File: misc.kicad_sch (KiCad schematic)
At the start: 23 parts, among them J7 Conn_ARM_JTAG_SWD_10, SW2 SW_DIP_x02, U1 MIMX8MM6DVTLZAA, Y3 24Mhz

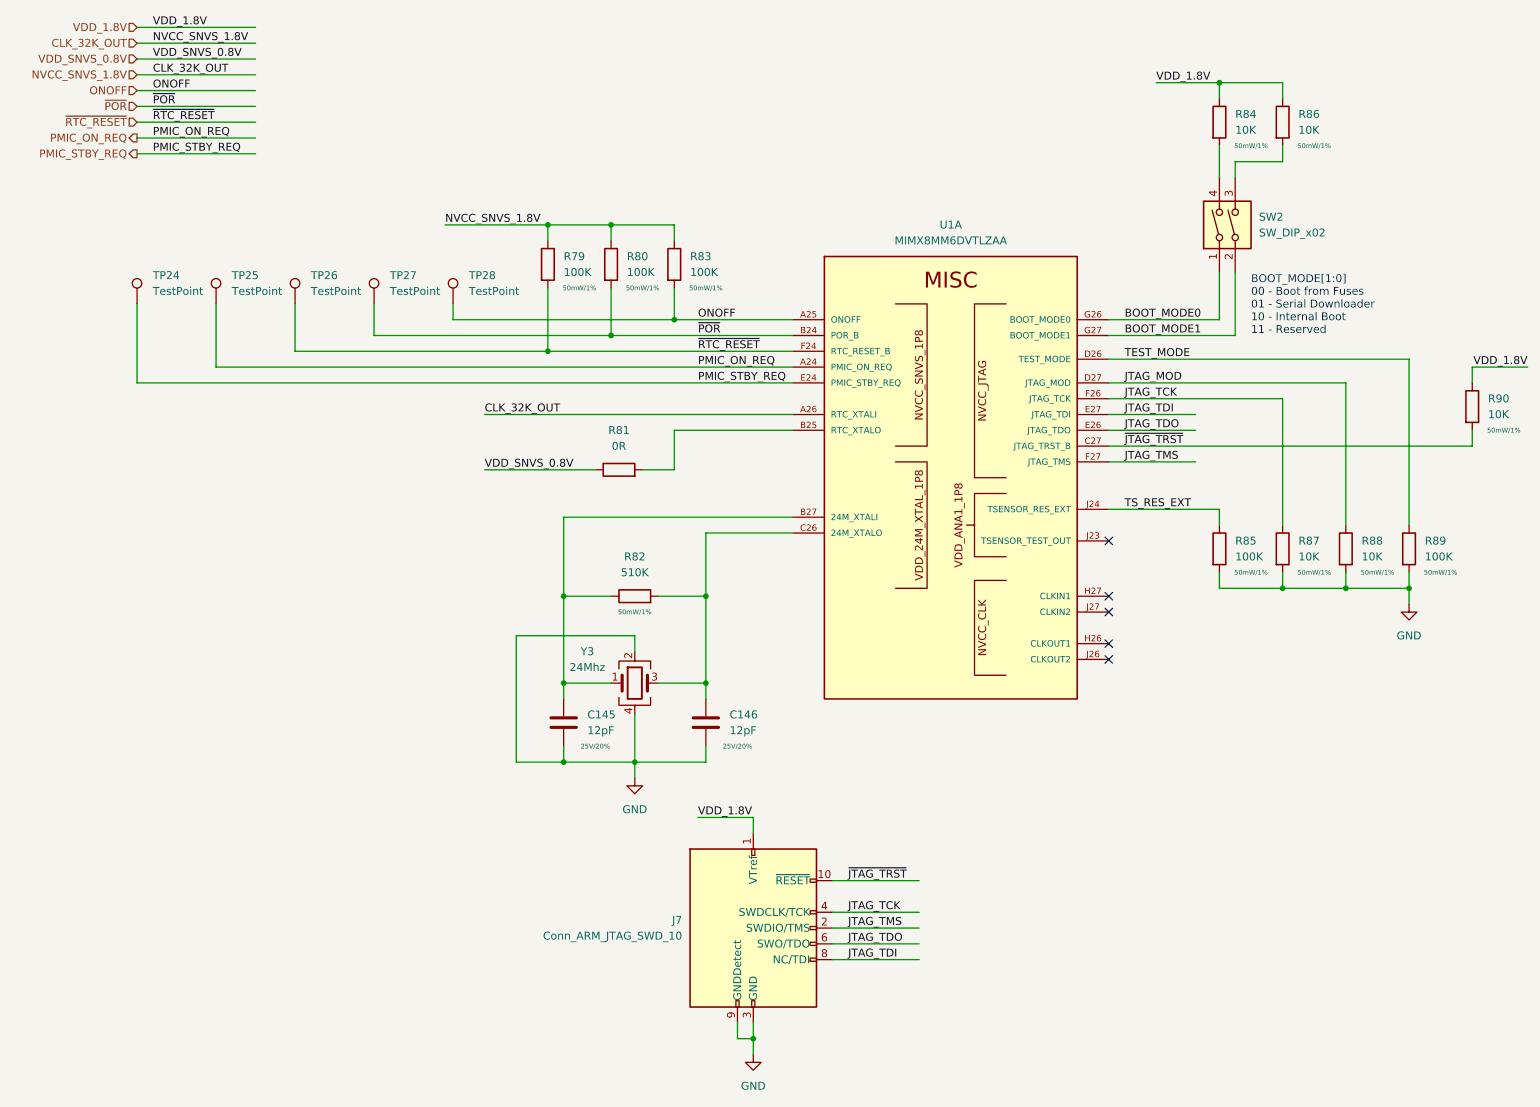
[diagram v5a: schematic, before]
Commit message: add inital ddr tool version, lots of routing work
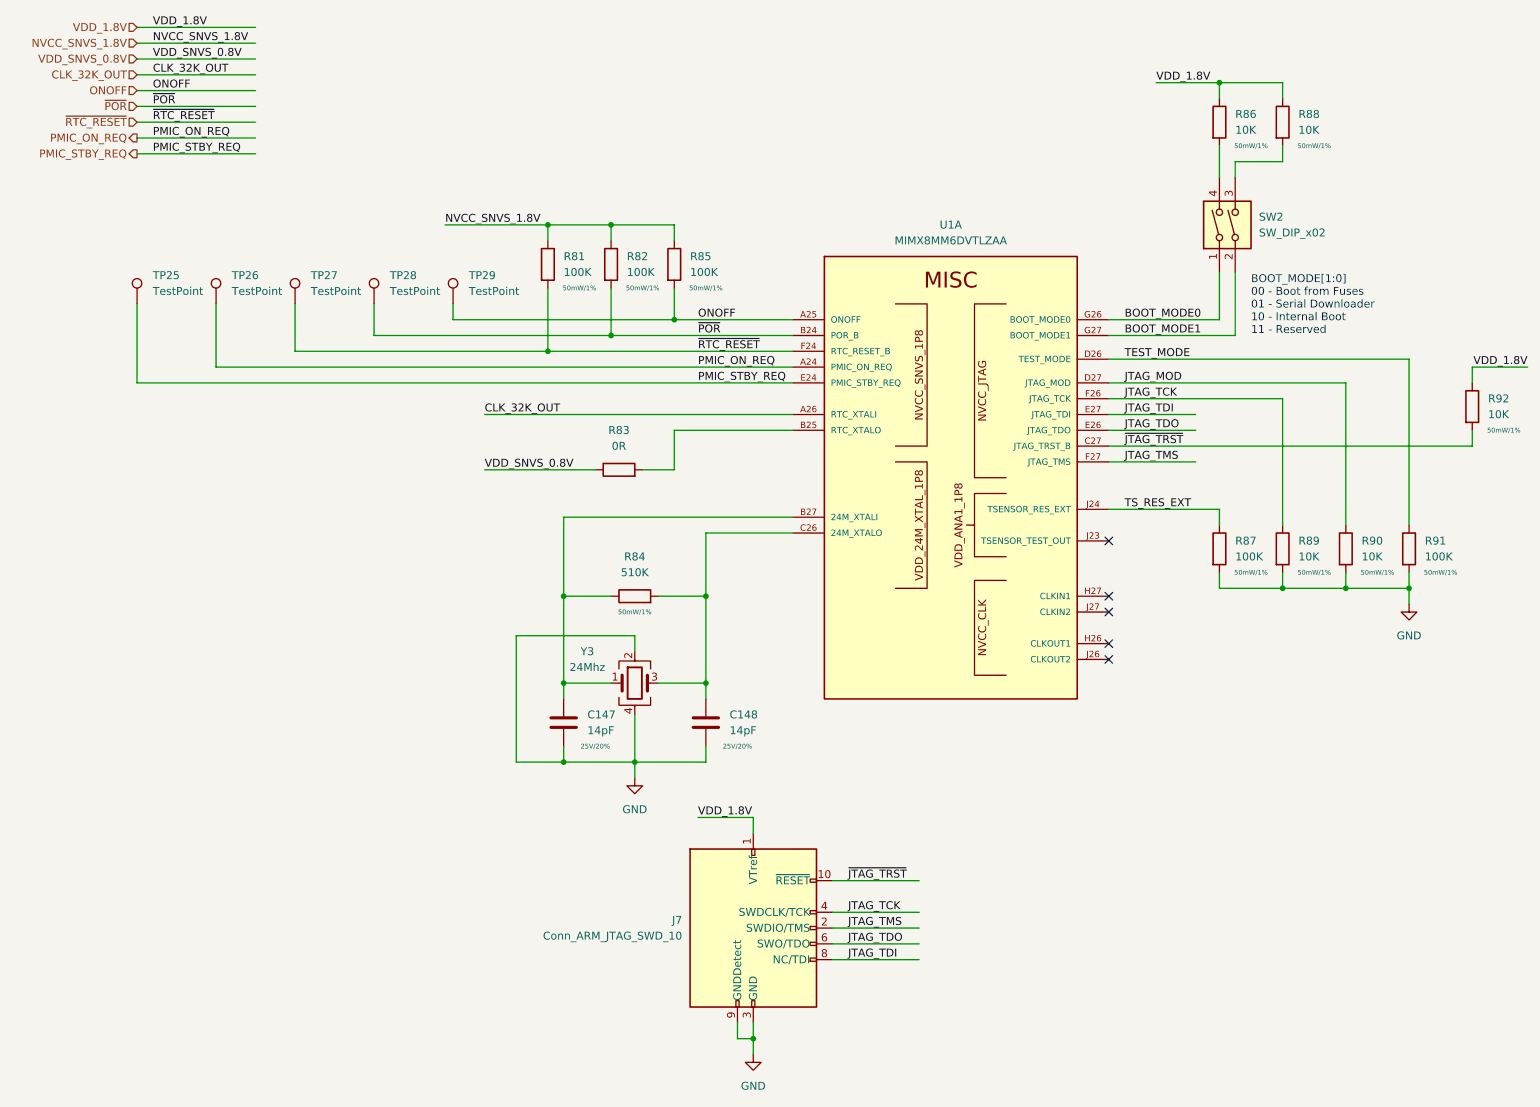
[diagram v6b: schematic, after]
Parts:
- C147: renamed from C145; value 12pF -> 14pF
- C148: renamed from C146; value 12pF -> 14pF
- Y3: MPN (none) -> ECS-240-10-33B-7KM-TR
- renumbered R79 to R81, R80 to R82, R81 to R83, R82 to R84, R83 to R85, R84 to R86, R85 to R87, R86 to R88, R87 to R89, R88 to R90, R89 to R91, R90 to R92, TP24 to TP25, TP25 to TP26, TP26 to TP27, TP27 to TP28, TP28 to TP29
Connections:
- net CLK_32K_OUT: no longer R81.1, R82.1, R85.1
- new net NVCC_SNVS_1.8V: R81.1, R82.1, R85.1
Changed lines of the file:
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@@
     (effects (font (size 1.27 1.27)) (justify right))
   )
-  (hierarchical_label "CLK_32K_OUT" (shape input) (at 30.48 22.86 180)
+  (hierarchical_label "CLK_32K_OUT" (shape input) (at 30.48 27.94 180)
     (effects (font (size 1.27 1.27)) (justify right))
   )
@@
     (effects (font (size 1.27 1.27)) (justify right))
   )
-  (hierarchical_label "NVCC_SNVS_1.8V" (shape input) (at 30.48 27.94 180)
+  (hierarchical_label "NVCC_SNVS_1.8V" (shape input) (at 30.48 22.86 180)
     (effects (font (size 1.27 1.27)) (justify right))
   )
@@
   (symbol (lib_id "Device:C") (at 99.06 132.08 0) (unit 1)
     (in_bom yes) (on_board yes)
-    (property "Reference" "C145" (id 0) (at 102.87 130.8099 0)
-      (effects (font (size 1.27 1.27)) (justify left))
-    )
-    (property "Value" "12pF" (id 1) (at 102.87 133.3499 0)
+    (property "Reference" "C147" (id 0) (at 102.87 130.8099 0)
+      (effects (font (size 1.27 1.27)) (justify left))
+    )
+    (property "Value" "14pF" (id 1) (at 102.87 133.3499 0)
       (effects (font (size 1.27 1.27)) (justify left))
     )
@@
   (symbol (lib_id "Device:R") (at 224.79 104.14 0) (unit 1)
     (in_bom yes) (on_board yes)
-    (property "Reference" "R88" (id 0) (at 227.33 102.8699 0)
+    (property "Reference" "R90" (id 0) (at 227.33 102.8699 0)
       (effects (font (size 1.27 1.27)) (justify left))
     )
@@
   (symbol (lib_id "Connector:TestPoint") (at 81.28 64.77 0) (unit 1)
     (in_bom yes) (on_board yes) (fields_autoplaced)
-    (property "Reference" "TP28" (id 0) (at 83.82 60.1979 0)
+    (property "Reference" "TP29" (id 0) (at 83.82 60.1979 0)
       (effects (font (size 1.27 1.27)) (justify left))
     )
@@
   (symbol (lib_id "power:GND") (at 129.54 185.42 0) (unit 1)
     (in_bom yes) (on_board yes) (fields_autoplaced)
-    (property "Reference" "#PWR0134" (id 0) (at 129.54 191.77 0)
+    (property "Reference" "#PWR0135" (id 0) (at 129.54 191.77 0)
       (effects (font (size 1.27 1.27)) hide)
     )
@@
   (symbol (lib_id "Device:R") (at 214.63 35.56 0) (unit 1)
     (in_bom yes) (on_board yes)
-    (property "Reference" "R86" (id 0) (at 217.17 34.2899 0)
+    (property "Reference" "R88" (id 0) (at 217.17 34.2899 0)
       (effects (font (size 1.27 1.27)) (justify left))
     )
@@
   (symbol (lib_id "Connector:TestPoint") (at 68.58 64.77 0) (unit 1)
     (in_bom yes) (on_board yes) (fields_autoplaced)
-    (property "Reference" "TP27" (id 0) (at 71.12 60.1979 0)
+    (property "Reference" "TP28" (id 0) (at 71.12 60.1979 0)
       (effects (font (size 1.27 1.27)) (justify left))
     )
@@
   (symbol (lib_id "Device:R") (at 204.47 35.56 0) (unit 1)
     (in_bom yes) (on_board yes)
-    (property "Reference" "R84" (id 0) (at 207.01 34.2899 0)
+    (property "Reference" "R86" (id 0) (at 207.01 34.2899 0)
       (effects (font (size 1.27 1.27)) (justify left))
     )
@@
   (symbol (lib_id "Device:R") (at 96.52 58.42 0) (unit 1)
     (in_bom yes) (on_board yes)
-    (property "Reference" "R79" (id 0) (at 99.06 57.1499 0)
+    (property "Reference" "R81" (id 0) (at 99.06 57.1499 0)
       (effects (font (size 1.27 1.27)) (justify left))
     )
@@
   (symbol (lib_id "Device:R") (at 110.49 111.76 90) (unit 1)
     (in_bom yes) (on_board yes)
-    (property "Reference" "R82" (id 0) (at 110.49 105.41 90))
+    (property "Reference" "R84" (id 0) (at 110.49 105.41 90))
     (property "Value" "510K" (id 1) (at 110.49 107.95 90))
     (property "Footprint" "Resistor_SMD:R_0402_1005Metric" (id 2) (at 110.49 113.538 90)
@@
   (symbol (lib_id "power:GND") (at 110.49 140.97 0) (unit 1)
     (in_bom yes) (on_board yes) (fields_autoplaced)
-    (property "Reference" "#PWR0133" (id 0) (at 110.49 147.32 0)
+    (property "Reference" "#PWR0134" (id 0) (at 110.49 147.32 0)
       (effects (font (size 1.27 1.27)) hide)
     )
@@
   (symbol (lib_id "Connector:TestPoint") (at 55.88 64.77 0) (unit 1)
     (in_bom yes) (on_board yes) (fields_autoplaced)
-    (property "Reference" "TP26" (id 0) (at 58.42 60.1979 0)
+    (property "Reference" "TP27" (id 0) (at 58.42 60.1979 0)
       (effects (font (size 1.27 1.27)) (justify left))
     )
@@
   (symbol (lib_id "Device:R") (at 234.95 104.14 0) (unit 1)
     (in_bom yes) (on_board yes)
-    (property "Reference" "R89" (id 0) (at 237.49 102.8699 0)
+    (property "Reference" "R91" (id 0) (at 237.49 102.8699 0)
       (effects (font (size 1.27 1.27)) (justify left))
     )
@@
   (symbol (lib_id "Device:R") (at 214.63 104.14 0) (unit 1)
     (in_bom yes) (on_board yes)
-    (property "Reference" "R87" (id 0) (at 217.17 102.8699 0)
+    (property "Reference" "R89" (id 0) (at 217.17 102.8699 0)
       (effects (font (size 1.27 1.27)) (justify left))
     )
@@
   (symbol (lib_id "Device:R") (at 116.84 58.42 0) (unit 1)
     (in_bom yes) (on_board yes)
-    (property "Reference" "R83" (id 0) (at 119.38 57.1499 0)
+    (property "Reference" "R85" (id 0) (at 119.38 57.1499 0)
       (effects (font (size 1.27 1.27)) (justify left))
     )
@@
   (symbol (lib_id "power:GND") (at 234.95 113.03 0) (unit 1)
     (in_bom yes) (on_board yes) (fields_autoplaced)
-    (property "Reference" "#PWR0135" (id 0) (at 234.95 119.38 0)
+    (property "Reference" "#PWR0136" (id 0) (at 234.95 119.38 0)
       (effects (font (size 1.27 1.27)) hide)
     )
@@
   (symbol (lib_id "Device:R") (at 204.47 104.14 0) (unit 1)
     (in_bom yes) (on_board yes)
-    (property "Reference" "R85" (id 0) (at 207.01 102.8699 0)
+    (property "Reference" "R87" (id 0) (at 207.01 102.8699 0)
       (effects (font (size 1.27 1.27)) (justify left))
     )
@@
   (symbol (lib_id "Device:C") (at 121.92 132.08 0) (unit 1)
     (in_bom yes) (on_board yes)
-    (property "Reference" "C146" (id 0) (at 125.73 130.8099 0)
-      (effects (font (size 1.27 1.27)) (justify left))
-    )
-    (property "Value" "12pF" (id 1) (at 125.73 133.3499 0)
+    (property "Reference" "C148" (id 0) (at 125.73 130.8099 0)
+      (effects (font (size 1.27 1.27)) (justify left))
+    )
+    (property "Value" "14pF" (id 1) (at 125.73 133.3499 0)
       (effects (font (size 1.27 1.27)) (justify left))
     )
@@
   (symbol (lib_id "Device:R") (at 245.11 81.28 0) (unit 1)
     (in_bom yes) (on_board yes)
-    (property "Reference" "R90" (id 0) (at 247.65 80.0099 0)
+    (property "Reference" "R92" (id 0) (at 247.65 80.0099 0)
       (effects (font (size 1.27 1.27)) (justify left))
     )
@@
   (symbol (lib_id "Connector:TestPoint") (at 30.48 64.77 0) (unit 1)
     (in_bom yes) (on_board yes) (fields_autoplaced)
-    (property "Reference" "TP24" (id 0) (at 33.02 60.1979 0)
+    (property "Reference" "TP25" (id 0) (at 33.02 60.1979 0)
       (effects (font (size 1.27 1.27)) (justify left))
     )
@@
   (symbol (lib_id "Device:R") (at 106.68 58.42 0) (unit 1)
     (in_bom yes) (on_board yes)
-    (property "Reference" "R80" (id 0) (at 109.22 57.1499 0)
+    (property "Reference" "R82" (id 0) (at 109.22 57.1499 0)
       (effects (font (size 1.27 1.27)) (justify left))
     )
@@
   (symbol (lib_id "Device:R") (at 107.95 91.44 90) (unit 1)
     (in_bom yes) (on_board yes) (fields_autoplaced)
-    (property "Reference" "R81" (id 0) (at 107.95 85.09 90))
+    (property "Reference" "R83" (id 0) (at 107.95 85.09 90))
     (property "Value" "0R" (id 1) (at 107.95 87.63 90))
     (property "Footprint" "Resistor_SMD:R_0402_1005Metric" (id 2) (at 107.95 93.218 90)
@@
       (effects (font (size 1.27 1.27)) hide)
     )
+    (property "MPN" "ECS-240-10-33B-7KM-TR" (id 4) (at 110.49 125.73 0)
+      (effects (font (size 1.27 1.27)) hide)
+    )
     (pin "1")
     (pin "2")
@@
   (symbol (lib_id "Connector:TestPoint") (at 43.18 64.77 0) (unit 1)
     (in_bom yes) (on_board yes) (fields_autoplaced)
-    (property "Reference" "TP25" (id 0) (at 45.72 60.1979 0)
-      (effects (font (size 1.27 1.27)) (justify left))
-    )
+    (property "Reference" "TP26" (id 0) (at 45.72 60.1979 0)
+      (effects (font (size 1.27 1.27)) (justify left))
+    )

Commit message: v2 of ddr flytimes tool, lots of routing work, sch fixes
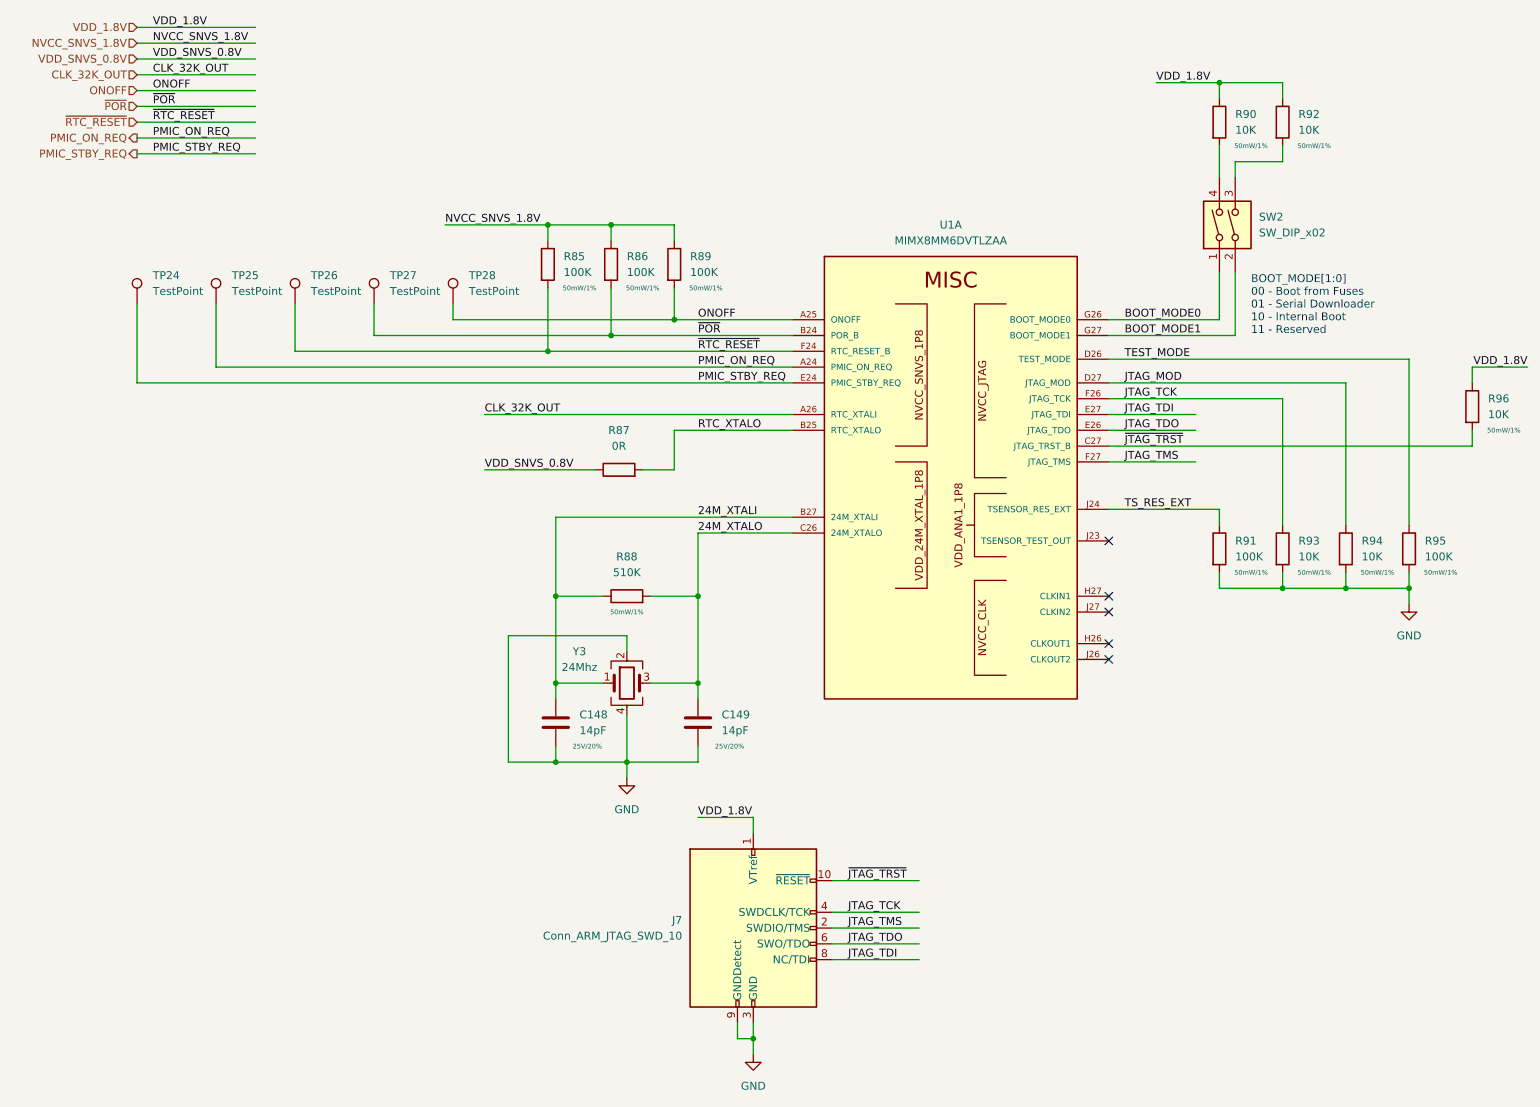
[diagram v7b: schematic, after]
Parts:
- renumbered C147 to C148, C148 to C149, R81 to R85, R82 to R86, R83 to R87, R84 to R88, R85 to R89, R86 to R90, R87 to R91, R88 to R92, R89 to R93, R90 to R94, R91 to R95, R92 to R96, TP25 to TP24, TP26 to TP25, TP27 to TP26, TP28 to TP27, TP29 to TP28
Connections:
- net 24M_XTALI: now reaches C148.1, R88.1, U1.B27 (24M_XTALI), Y3.1
- net RTC_XTALO: now reaches R87.2, U1.B25 (RTC_XTALO)
- net 24M_XTALO: now reaches C149.1, R88.2, U1.C26 (24M_XTALO), Y3.3
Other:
- moved on the sheet: C148, C149, R88, Y3
